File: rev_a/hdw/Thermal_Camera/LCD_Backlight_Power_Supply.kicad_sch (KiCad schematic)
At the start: 13 parts

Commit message: lots of schematic progress
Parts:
- C1202: renamed from C?; footprint Capacitors_SMD:C_0603 -> (none); display_footprint 0603 -> (none)
- R1202, R1203: renamed from R?; footprint Resistors_SMD:R_0603 -> (none); Wattage 1/10W -> (none); display_footprint 0603 -> (none)
- R? (x2): footprint Resistors_SMD:R_0603 -> (none); Digi-Key PN 541-10.0HCT-ND -> (none); Wattage 1/10W -> (none); display_footprint 0603 -> (none)
- R?: renamed from R1501; footprint Resistors_SMD:R_0603 -> (none); Digi-Key PN 541-10.0KHCT-ND -> (none); Wattage 1/10W -> (none); display_footprint 0603 -> (none)
- gave numbers to parts that had none: 6

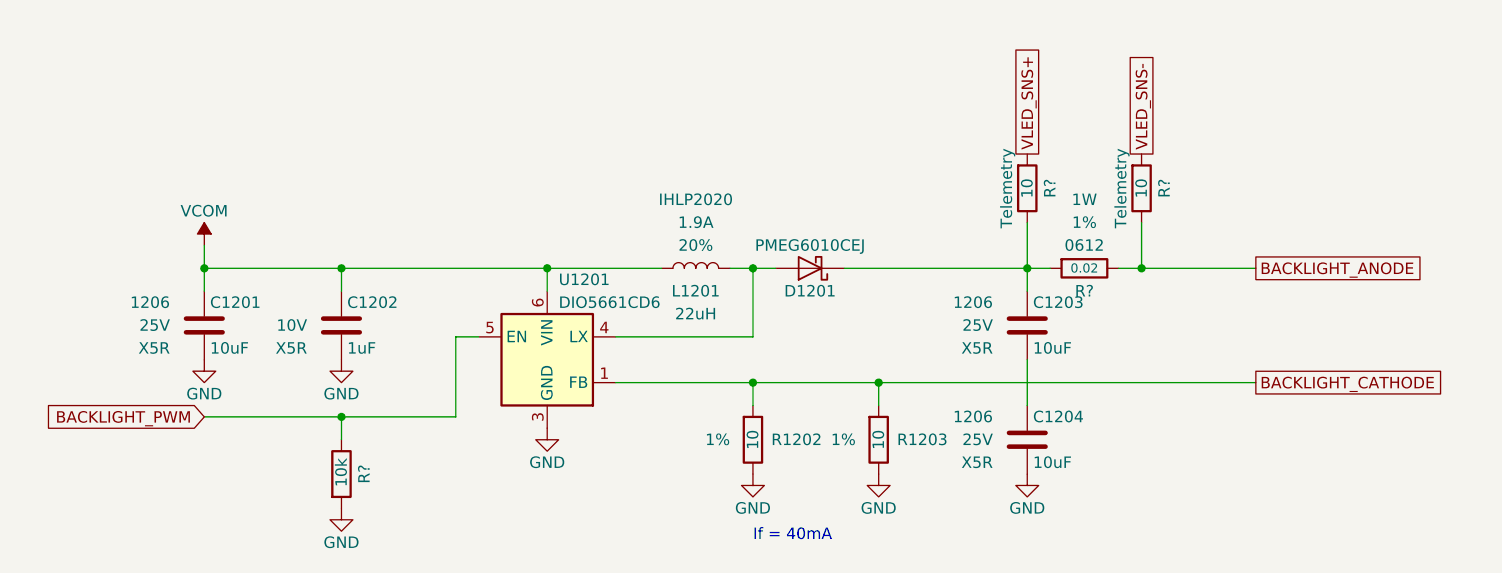
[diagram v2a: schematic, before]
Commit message: assigned a ton of footprints
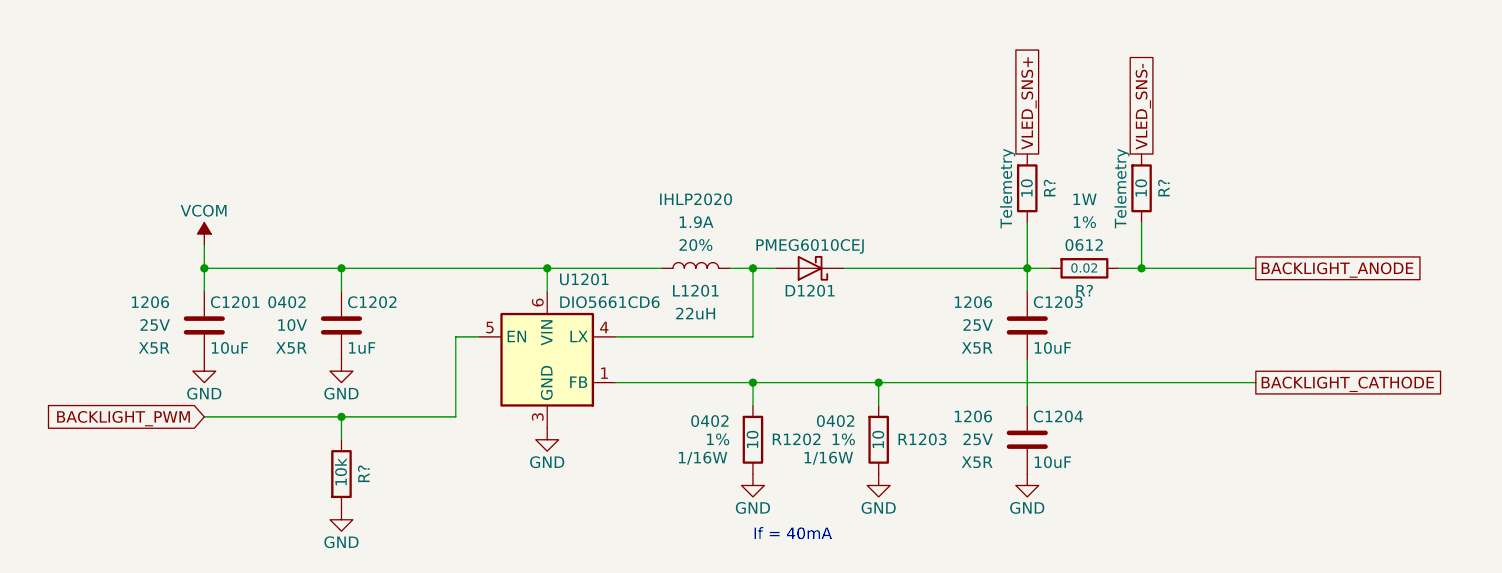
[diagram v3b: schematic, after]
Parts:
- C1202: footprint (none) -> Capacitors_SMD:C_0402; display_footprint (none) -> 0402
- D1201: Digi-Key PN (none) -> 1727-3882-1-ND
- R1202, R1203, R? (x3): footprint (none) -> Resistors_SMD:R_0402; Wattage (none) -> 1/16W; display_footprint (none) -> 0402
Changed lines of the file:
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@@
 			)
 		)
-		(property "Footprint" ""
+		(property "Footprint" "Resistors_SMD:R_0402"
 			(at 170.18 66.04 0)
 			(effects
@@
 			)
 		)
-		(property "display_footprint" ""
+		(property "display_footprint" "0402"
 			(at 167.64 66.04 90)
 			(effects
@@
 			)
 		)
-		(property "Wattage" ""
+		(property "Wattage" "1/16W"
 			(at 162.56 66.04 90)
 			(effects
@@
 			)
 		)
-		(property "Footprint" ""
+		(property "Footprint" "Resistors_SMD:R_0402"
 			(at 139.7 93.98 0)
 			(effects
@@
 			)
 		)
-		(property "display_footprint" ""
+		(property "display_footprint" "0402"
 			(at 137.16 91.948 0)
 			(effects
@@
 			)
 		)
-		(property "Wattage" ""
+		(property "Wattage" "1/16W"
 			(at 136.906 96.012 0)
 			(effects
@@
 			)
 		)
-		(property "Footprint" ""
+		(property "Footprint" "Resistors_SMD:R_0402"
 			(at 153.67 93.98 0)
 			(effects
@@
 			)
 		)
-		(property "display_footprint" ""
+		(property "display_footprint" "0402"
 			(at 151.13 91.948 0)
 			(effects
@@
 			)
 		)
-		(property "Wattage" ""
+		(property "Wattage" "1/16W"
 			(at 150.876 96.012 0)
 			(effects
@@
 			)
 		)
-		(property "Footprint" ""
+		(property "Footprint" "Resistors_SMD:R_0402"
 			(at 182.88 66.04 0)
 			(effects
@@
 			)
 		)
-		(property "display_footprint" ""
+		(property "display_footprint" "0402"
 			(at 180.34 66.04 90)
 			(effects
@@
 			)
 		)
-		(property "Wattage" ""
+		(property "Wattage" "1/16W"
 			(at 175.26 66.04 90)
 			(effects
@@
 			)
 		)
-		(property "Footprint" ""
+		(property "Footprint" "Resistors_SMD:R_0402"
 			(at 93.98 97.79 0)
 			(effects
@@
 			)
 		)
-		(property "display_footprint" ""
+		(property "display_footprint" "0402"
 			(at 91.44 99.568 0)
 			(effects
@@
 			)
 		)
-		(property "Wattage" ""
+		(property "Wattage" "1/16W"
 			(at 91.44 94.488 0)
 			(effects
@@
 			)
 		)
-		(property "Footprint" ""
+		(property "Footprint" "Capacitors_SMD:C_0402"
 			(at 94.9452 85.09 0)
 			(effects
@@
 			)
 		)
-		(property "display_footprint" ""
+		(property "display_footprint" "0402"
 			(at 90.17 78.74 0)
 			(effects
@@
 			(at 146.05 74.93 0)
 			(effects
+				(font
+					(size 1.27 1.27)
+				)
+				(hide yes)
+			)
+		)
+		(property "Digi-Key PN" "1727-3882-1-ND"
+			(at 146.05 74.93 0)
+			(effects

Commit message: assigned some part numbers
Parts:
- C1202: Digi-Key PN (none) -> 311-1439-1-ND
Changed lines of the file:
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@@
 			)
 		)
-		(property "Digi-Key PN" ""
+		(property "Digi-Key PN" "311-1439-1-ND"
 			(at 93.98 81.28 0)
 			(effects

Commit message: assigned resistor part numbers
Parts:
- R1202, R1203, R? (x2): Digi-Key PN (none) -> RMCF0402FT10R0CT-ND
- R?: Digi-Key PN (none) -> RMCF0402FT10K0CT-ND
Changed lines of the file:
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@@
 			)
 		)
-		(property "Digi-Key PN" ""
+		(property "Digi-Key PN" "RMCF0402FT10R0CT-ND"
 			(at 170.18 66.04 0)
 			(effects
@@
 			)
 		)
-		(property "Digi-Key PN" ""
+		(property "Digi-Key PN" "RMCF0402FT10R0CT-ND"
 			(at 132.08 83.82 0)
 			(effects
@@
 			)
 		)
-		(property "Digi-Key PN" ""
+		(property "Digi-Key PN" "RMCF0402FT10R0CT-ND"
 			(at 146.05 83.82 0)
 			(effects
@@
 			)
 		)
-		(property "Digi-Key PN" ""
+		(property "Digi-Key PN" "RMCF0402FT10R0CT-ND"
 			(at 182.88 66.04 0)
 			(effects
@@
 			)
 		)
-		(property "Digi-Key PN" ""
+		(property "Digi-Key PN" "RMCF0402FT10K0CT-ND"
 			(at 86.36 107.95 0)
 			(effects
